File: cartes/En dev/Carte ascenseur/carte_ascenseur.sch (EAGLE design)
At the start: 22 parts, among them U1 MCP2551, U2 ADUM1250ARZ, U3 ADUM1400ARWZ

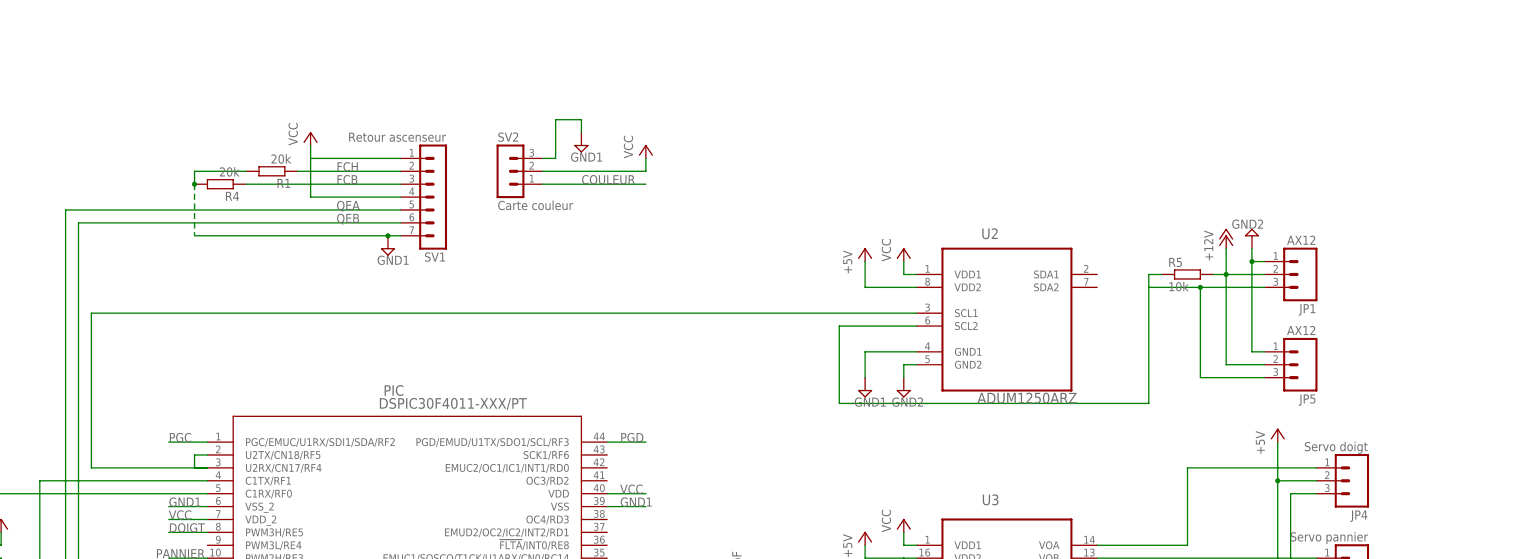
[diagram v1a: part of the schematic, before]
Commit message: Correction
Ajout de la connexion à l'alim 'dirty' et d'un LM7805 pour faire du 5V
dirty au cas où.
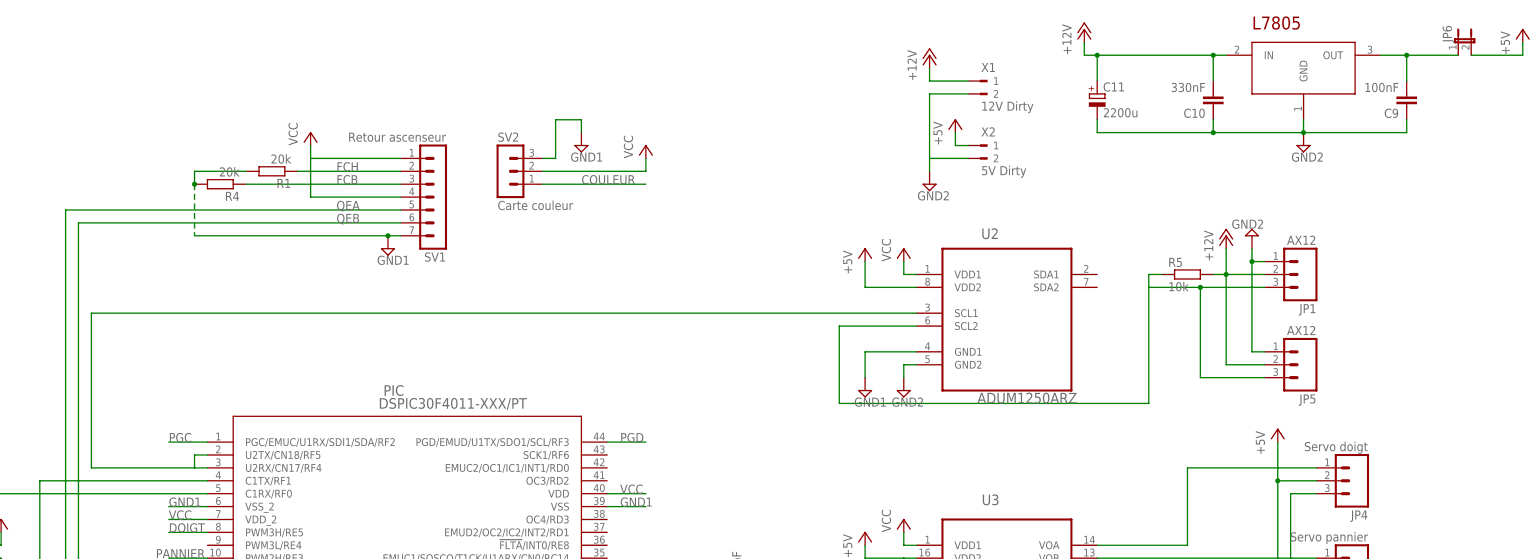
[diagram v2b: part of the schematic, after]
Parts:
- added C10: 330nF, rcl:C-EUC0805
- added C11: 2200u, rcl:CPOL-EUTT5D11
- added C9: 100nF, rcl:C-EUC0805
- added JP6: (no value), jumper:JP1E
- added U$5: L7805TO263, st-microelectronics:L7805TO263
- added X1: 12V Dirty, con-weidmueller-sl35:90-2
- added X2: 5V Dirty, con-weidmueller-sl35:90-2
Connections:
- new net N$6: C9.2, JP6.1, U$5.OUT
- net +12V: now also C10.2, C11.+, U$5.IN, X1.1
- net +5V: now also JP6.2, X2.1
- net GND2: now also C10.1, C11.-, C9.1, U$5.GND, X1.2, X2.2
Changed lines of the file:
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@@
 <part name="JP5" library="SparkFun-Connectors" deviceset="M03" device="POLAR" value="AX12"/>
 <part name="P+3" library="supply1" deviceset="VCC" device=""/>
+<part name="U$5" library="st-microelectronics" deviceset="L7805" device="TO263"/>
+<part name="C9" library="rcl" deviceset="C-EU" device="C0805" value="100nF"/>
+<part name="C10" library="rcl" deviceset="C-EU" device="C0805" value="330nF"/>
+<part name="C11" library="rcl" deviceset="CPOL-EU" device="TT5D11" value="2200u"/>
+<part name="SUPPLY9" library="supply2" deviceset="GND2" device=""/>
+<part name="P+14" library="supply1" deviceset="+12V" device=""/>
+<part name="P+15" library="supply1" deviceset="+5V" device=""/>
+<part name="X1" library="con-weidmueller-sl35" deviceset="90-2" device="" value="12V Dirty"/>
+<part name="X2" library="con-weidmueller-sl35" deviceset="90-2" device="" value="5V Dirty">
+<attribute name="MF" value=""/>
+<attribute name="MPN" value=""/>
+<attribute name="OC_FARNELL" value="unknown"/>
+<attribute name="OC_NEWARK" value="unknown"/>
+</part>
+<part name="P+16" library="supply1" deviceset="+12V" device=""/>
+<part name="SUPPLY12" library="supply2" deviceset="GND2" device=""/>
+<part name="P+17" library="supply1" deviceset="+5V" device=""/>
+<part name="JP6" library="jumper" deviceset="JP1E" device=""/>
 </parts>
 <sheets>
@@
 <instance part="JP5" gate="G$1" x="256.54" y="91.44" rot="R180"/>
 <instance part="P+3" gate="VCC" x="0" y="60.96"/>
+<instance part="U$5" gate="G$1" x="256.54" y="149.86"/>
+<instance part="C9" gate="G$1" x="276.86" y="142.24" rot="R180"/>
+<instance part="C10" gate="G$1" x="238.76" y="142.24" rot="R180"/>
+<instance part="C11" gate="G$1" x="215.9" y="144.78"/>
+<instance part="SUPPLY9" gate="G$1" x="256.54" y="134.62"/>
+<instance part="P+14" gate="1" x="213.36" y="157.48"/>
+<instance part="P+15" gate="1" x="299.72" y="157.48"/>
+<instance part="X1" gate="G$1" x="193.04" y="147.32"/>
+<instance part="X2" gate="G$1" x="193.04" y="134.62"/>
+<instance part="P+16" gate="1" x="182.88" y="152.4"/>
+<instance part="SUPPLY12" gate="G$1" x="182.88" y="127"/>
+<instance part="P+17" gate="1" x="187.96" y="139.7"/>
+<instance part="JP6" gate="A" x="287.02" y="154.94"/>
 </instances>
 <busses>
@@
 <junction x="251.46" y="50.8"/>
 </segment>
+<segment>
+<pinref part="X2" gate="G$1" pin="1"/>
+<wire x1="190.5" y1="134.62" x2="187.96" y2="134.62" width="0.1524" layer="91"/>
+<wire x1="187.96" y1="134.62" x2="187.96" y2="137.16" width="0.1524" layer="91"/>
+<pinref part="P+17" gate="1" pin="+5V"/>
+</segment>
+<segment>
+<pinref part="JP6" gate="A" pin="2"/>
+<pinref part="P+15" gate="1" pin="+5V"/>
+<wire x1="289.56" y1="152.4" x2="299.72" y2="152.4" width="0.1524" layer="91"/>
+<wire x1="299.72" y1="152.4" x2="299.72" y2="154.94" width="0.1524" layer="91"/>
+</segment>
 </net>
 <net name="GND1" class="0">
@@
 <junction x="254" y="30.48"/>
 </segment>
+<segment>
+<pinref part="C9" gate="G$1" pin="1"/>
+<wire x1="276.86" y1="139.7" x2="276.86" y2="137.16" width="0.1524" layer="91"/>
+<wire x1="276.86" y1="137.16" x2="256.54" y2="137.16" width="0.1524" layer="91"/>
+<pinref part="U$5" gate="G$1" pin="GND"/>
+<wire x1="256.54" y1="139.7" x2="256.54" y2="137.16" width="0.1524" layer="91"/>
+<pinref part="C10" gate="G$1" pin="1"/>
+<wire x1="256.54" y1="137.16" x2="238.76" y2="137.16" width="0.1524" layer="91"/>
+<wire x1="238.76" y1="137.16" x2="238.76" y2="139.7" width="0.1524" layer="91"/>
+<junction x="256.54" y="137.16"/>
+<pinref part="C11" gate="G$1" pin="-"/>
+<wire x1="215.9" y1="139.7" x2="215.9" y2="137.16" width="0.1524" layer="91"/>
+<wire x1="215.9" y1="137.16" x2="238.76" y2="137.16" width="0.1524" layer="91"/>
+<junction x="238.76" y="137.16"/>
+<pinref part="SUPPLY9" gate="G$1" pin="GND2"/>
+</segment>
+<segment>
+<pinref part="X1" gate="G$1" pin="2"/>
+<wire x1="190.5" y1="144.78" x2="182.88" y2="144.78" width="0.1524" layer="91"/>
+<wire x1="182.88" y1="144.78" x2="182.88" y2="132.08" width="0.1524" layer="91"/>
+<pinref part="X2" gate="G$1" pin="2"/>
+<wire x1="190.5" y1="132.08" x2="182.88" y2="132.08" width="0.1524" layer="91"/>
+<wire x1="182.88" y1="132.08" x2="182.88" y2="129.54" width="0.1524" layer="91"/>
+<pinref part="SUPPLY12" gate="G$1" pin="GND2"/>
+</segment>
 </net>
 <net name="N$1" class="0">
@@
 <wire x1="38.1" y1="73.66" x2="38.1" y2="71.12" width="0.1524" layer="91"/>
 <pinref part="PIC" gate="A" pin="U2RX/CN17/RF4"/>
-<wire x1="38.1" y1="71.12" x2="40.64" y2="71.12" width="0.1524" layer="91"/>
-<wire x1="40.64" y1="71.12" x2="17.78" y2="71.12" width="0.1524" layer="91"/>
+<wire x1="40.64" y1="71.12" x2="38.1" y2="71.12" width="0.1524" layer="91"/>
+<wire x1="38.1" y1="71.12" x2="17.78" y2="71.12" width="0.1524" layer="91"/>
 <wire x1="17.78" y1="71.12" x2="17.78" y2="101.6" width="0.1524" layer="91"/>
 <pinref part="U2" gate="A" pin="SCL1"/>
@@
 <wire x1="241.3" y1="109.22" x2="238.76" y2="109.22" width="0.1524" layer="91"/>
 </segment>
-</net>
+<segment>
+<pinref part="U$5" gate="G$1" pin="IN"/>
+<wire x1="241.3" y1="152.4" x2="238.76" y2="152.4" width="0.1524" layer="91"/>
+<pinref part="C10" gate="G$1" pin="2"/>
+<wire x1="238.76" y1="152.4" x2="215.9" y2="152.4" width="0.1524" layer="91"/>
+<wire x1="215.9" y1="152.4" x2="213.36" y2="152.4" width="0.1524" layer="91"/>
+<wire x1="238.76" y1="147.32" x2="238.76" y2="152.4" width="0.1524" layer="91"/>
+<junction x="238.76" y="152.4"/>
+<pinref part="C11" gate="G$1" pin="+"/>
+<wire x1="215.9" y1="147.32" x2="215.9" y2="152.4" width="0.1524" layer="91"/>
+<junction x="215.9" y="152.4"/>
+<pinref part="P+14" gate="1" pin="+12V"/>
+<wire x1="213.36" y1="154.94" x2="213.36" y2="152.4" width="0.1524" layer="91"/>
+</segment>
+<segment>
+<pinref part="X1" gate="G$1" pin="1"/>
+<wire x1="190.5" y1="147.32" x2="182.88" y2="147.32" width="0.1524" layer="91"/>
+<wire x1="182.88" y1="147.32" x2="182.88" y2="149.86" width="0.1524" layer="91"/>
+<pinref part="P+16" gate="1" pin="+12V"/>
+</segment>
+</net>
+<net name="N$6" class="0">
+<segment>
+<pinref part="U$5" gate="G$1" pin="OUT"/>
+<wire x1="271.78" y1="152.4" x2="276.86" y2="152.4" width="0.1524" layer="91"/>
+<pinref part="C9" gate="G$1" pin="2"/>
+<wire x1="276.86" y1="152.4" x2="287.02" y2="152.4" width="0.1524" layer="91"/>
+<wire x1="276.86" y1="147.32" x2="276.86" y2="152.4" width="0.1524" layer="91"/>
+<junction x="276.86" y="152.4"/>
+<pinref part="JP6" gate="A" pin="1"/>
+</segment>
+</net>

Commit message: Correction carte ascenseur
Ajout des leds d'indication de présence de tension, 5V, 5V dirty, 12V
dirty
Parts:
- added LED_12V, LED_5V, LED_5V1: (no value), adafruit:LEDCHIPLED_0805
- added R6, R7, R8: 1k, SparkFun-Passives:RESISTOR0805-RES
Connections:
- new net N$11: LED_12V.A, R7.2
- new net N$12: LED_5V1.A, R8.2
- new net N$2: LED_5V.A, R6.2
- new net N$5: LED_12V.C, LED_5V.C
- net +12V: now also R7.1
- net +5V: now also R6.1
- net DOIGT: now also U3.VIB; no longer U3.VIA
- net GND1: now also LED_5V1.C
- net LANCEUR: now also U3.VIA; no longer U3.VIC
- net PANNIER: now also U3.VIC; no longer U3.VIB
- net VCC: now also R8.1
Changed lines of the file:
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@@
 <layer number="54" name="bGND_GNDA" color="1" fill="9" visible="no" active="no"/>
 <layer number="56" name="wert" color="7" fill="1" visible="no" active="no"/>
+<layer number="57" name="tCAD" color="7" fill="1" visible="no" active="no"/>
 <layer number="91" name="Nets" color="2" fill="1" visible="yes" active="yes"/>
 <layer number="92" name="Busses" color="1" fill="1" visible="yes" active="yes"/>
@@
 <layer number="108" name="tplace-old" color="10" fill="1" visible="yes" active="yes"/>
 <layer number="109" name="ref-old" color="11" fill="1" visible="yes" active="yes"/>
+<layer number="110" name="fp0" color="7" fill="1" visible="no" active="yes"/>
+<layer number="111" name="LPC17xx" color="7" fill="1" visible="yes" active="yes"/>
+<layer number="112" name="tSilk" color="7" fill="1" visible="yes" active="yes"/>
 <layer number="116" name="Patch_BOT" color="9" fill="4" visible="yes" active="yes"/>
 <layer number="121" name="_tsilk" color="7" fill="1" visible="yes" active="yes"/>
 <layer number="122" name="_bsilk" color="7" fill="1" visible="yes" active="yes"/>
+<layer number="123" name="tTestmark" color="7" fill="1" visible="no" active="yes"/>
+<layer number="124" name="bTestmark" color="7" fill="1" visible="no" active="yes"/>
 <layer number="125" name="_tNames" color="7" fill="1" visible="yes" active="yes"/>
+<layer number="126" name="_bNames" color="7" fill="1" visible="yes" active="yes"/>
+<layer number="127" name="_tValues" color="7" fill="1" visible="yes" active="yes"/>
+<layer number="128" name="_bValues" color="7" fill="1" visible="yes" active="yes"/>
+<layer number="131" name="tAdjust" color="7" fill="1" visible="no" active="yes"/>
+<layer number="132" name="bAdjust" color="7" fill="1" visible="no" active="yes"/>
 <layer number="144" name="Drill_legend" color="7" fill="1" visible="yes" active="yes"/>
+<layer number="150" name="Notes" color="7" fill="1" visible="no" active="yes"/>
 <layer number="151" name="HeatSink" color="7" fill="1" visible="yes" active="yes"/>
+<layer number="152" name="_bDocu" color="7" fill="1" visible="yes" active="yes"/>
+<layer number="153" name="FabDoc1" color="6" fill="1" visible="no" active="no"/>
+<layer number="154" name="FabDoc2" color="2" fill="1" visible="no" active="no"/>
+<layer number="155" name="FabDoc3" color="7" fill="15" visible="no" active="no"/>
 <layer number="199" name="Contour" color="7" fill="1" visible="yes" active="yes"/>
 <layer number="200" name="200bmp" color="1" fill="10" visible="no" active="no"/>
@@
 <layer number="223" name="223bmp" color="24" fill="1" visible="no" active="no"/>
 <layer number="224" name="224bmp" color="25" fill="1" visible="no" active="no"/>
+<layer number="248" name="Housing" color="7" fill="1" visible="yes" active="yes"/>
+<layer number="249" name="Edge" color="7" fill="1" visible="yes" active="yes"/>
 <layer number="250" name="Descript" color="3" fill="1" visible="no" active="no"/>
 <layer number="251" name="SMDround" color="12" fill="11" visible="no" active="no"/>
@@
 <part name="P+17" library="supply1" deviceset="+5V" device=""/>
 <part name="JP6" library="jumper" deviceset="JP1E" device=""/>
+<part name="LED_5V" library="adafruit" deviceset="LED" device="CHIPLED_0805"/>
+<part name="R6" library="SparkFun-Passives" deviceset="RESISTOR" device="0805-RES" value="1k">
+<attribute name="MF" value=""/>
+<attribute name="MPN" value=""/>
+<attribute name="OC_FARNELL" value="unknown"/>
+</part>
+<part name="P+18" library="supply1" deviceset="+5V" device=""/>
+<part name="SUPPLY16" library="supply2" deviceset="GND2" device=""/>
+<part name="LED_12V" library="adafruit" deviceset="LED" device="CHIPLED_0805"/>
+<part name="R7" library="SparkFun-Passives" deviceset="RESISTOR" device="0805-RES" value="1k">
+<attribute name="MF" value=""/>
+<attribute name="MPN" value=""/>
+<attribute name="OC_FARNELL" value="unknown"/>
+</part>
+<part name="P+19" library="supply1" deviceset="+12V" device=""/>
+<part name="LED_5V1" library="adafruit" deviceset="LED" device="CHIPLED_0805"/>
+<part name="R8" library="SparkFun-Passives" deviceset="RESISTOR" device="0805-RES" value="1k">
+<attribute name="MF" value=""/>
+<attribute name="MPN" value=""/>
+<attribute name="OC_FARNELL" value="unknown"/>
+</part>
+<part name="P+20" library="supply1" deviceset="VCC" device=""/>
+<part name="SUPPLY18" library="supply2" deviceset="GND1" device=""/>
 </parts>
 <sheets>
@@
 <instance part="P+17" gate="1" x="187.96" y="139.7"/>
 <instance part="JP6" gate="A" x="287.02" y="154.94"/>
+<instance part="LED_5V" gate="G$1" x="317.5" y="111.76"/>
+<instance part="R6" gate="G$1" x="317.5" y="121.92" rot="R270">
+<attribute name="OC_FARNELL" x="317.5" y="121.92" size="1.778" layer="96" rot="R180" display="off"/>
+<attribute name="MF" x="317.5" y="121.92" size="1.778" layer="96" rot="R180" display="off"/>
+<attribute name="MPN" x="317.5" y="121.92" size="1.778" layer="96" rot="R180" display="off"/>
+</instance>
+<instance part="P+18" gate="1" x="317.5" y="134.62"/>
+<instance part="SUPPLY16" gate="G$1" x="317.5" y="99.06"/>
+<instance part="LED_12V" gate="G$1" x="330.2" y="111.76"/>
+<instance part="R7" gate="G$1" x="330.2" y="121.92" rot="R270">
+<attribute name="OC_FARNELL" x="330.2" y="121.92" size="1.778" layer="96" rot="R180" display="off"/>
+<attribute name="MF" x="330.2" y="121.92" size="1.778" layer="96" rot="R180" display="off"/>
+<attribute name="MPN" x="330.2" y="121.92" size="1.778" layer="96" rot="R180" display="off"/>
+</instance>
+<instance part="P+19" gate="1" x="330.2" y="134.62"/>
+<instance part="LED_5V1" gate="G$1" x="-104.14" y="48.26"/>
+<instance part="R8" gate="G$1" x="-104.14" y="58.42" rot="R270">
+<attribute name="OC_FARNELL" x="-104.14" y="58.42" size="1.778" layer="96" rot="R180" display="off"/>
+<attribute name="MF" x="-104.14" y="58.42" size="1.778" layer="96" rot="R180" display="off"/>
+<attribute name="MPN" x="-104.14" y="58.42" size="1.778" layer="96" rot="R180" display="off"/>
+</instance>
+<instance part="P+20" gate="VCC" x="-104.14" y="68.58"/>
+<instance part="SUPPLY18" gate="G$1" x="-104.14" y="38.1"/>
 </instances>
 <busses>
@@
 <wire x1="299.72" y1="152.4" x2="299.72" y2="154.94" width="0.1524" layer="91"/>
 </segment>
+<segment>
+<pinref part="R6" gate="G$1" pin="1"/>
+<wire x1="317.5" y1="127" x2="317.5" y2="132.08" width="0.1524" layer="91"/>
+<pinref part="P+18" gate="1" pin="+5V"/>
+</segment>
 </net>
 <net name="GND1" class="0">
@@
 <wire x1="-7.62" y1="53.34" x2="0" y2="53.34" width="0.1524" layer="91"/>
 <wire x1="0" y1="53.34" x2="0" y2="50.8" width="0.1524" layer="91"/>
+</segment>
+<segment>
+<pinref part="LED_5V1" gate="G$1" pin="C"/>
+<wire x1="-104.14" y1="43.18" x2="-104.14" y2="40.64" width="0.1524" layer="91"/>
+<pinref part="SUPPLY18" gate="G$1" pin="GND1"/>
 </segment>
 </net>
@@
 <pinref part="U1" gate="G$1" pin="VDD"/>
 <wire x1="-5.08" y1="55.88" x2="-7.62" y2="55.88" width="0.1524" layer="91"/>
+</segment>
+<segment>
+<pinref part="P+20" gate="VCC" pin="VCC"/>
+<pinref part="R8" gate="G$1" pin="1"/>
+<wire x1="-104.14" y1="66.04" x2="-104.14" y2="63.5" width="0.1524" layer="91"/>
 </segment>
 </net>
@@
 </segment>
 <segment>
-<pinref part="U3" gate="A" pin="VIA"/>
-<wire x1="180.34" y1="43.18" x2="172.72" y2="43.18" width="0.1524" layer="91"/>
-<label x="172.72" y="43.18" size="1.778" layer="96"/>
+<label x="167.64" y="40.64" size="1.778" layer="96"/>
+<pinref part="U3" gate="A" pin="VIB"/>
+<wire x1="167.64" y1="40.64" x2="180.34" y2="40.64" width="0.1524" layer="91"/>
 </segment>
 </net>
@@
 </segment>
 <segment>
-<pinref part="U3" gate="A" pin="VIB"/>
-<wire x1="180.34" y1="40.64" x2="172.72" y2="40.64" width="0.1524" layer="91"/>
-<label x="170.18" y="40.64" size="1.778" layer="96"/>
+<pinref part="U3" gate="A" pin="VIC"/>
+<wire x1="167.64" y1="38.1" x2="180.34" y2="38.1" width="0.1524" layer="91"/>
+<label x="167.64" y="38.1" size="1.778" layer="95"/>
 </segment>
 </net>
 <net name="LANCEUR" class="0">
 <segment>
-<pinref part="U3" gate="A" pin="VIC"/>
-<wire x1="180.34" y1="38.1" x2="172.72" y2="38.1" width="0.1524" layer="91"/>
-<label x="170.18" y="38.1" size="1.778" layer="96"/>
+<label x="167.64" y="43.18" size="1.778" layer="96"/>
+<pinref part="U3" gate="A" pin="VIA"/>
+<wire x1="167.64" y1="43.18" x2="180.34" y2="43.18" width="0.1524" layer="91"/>
 </segment>
 <segment>
@@
 <pinref part="P+16" gate="1" pin="+12V"/>
 </segment>
+<segment>
+<pinref part="P+19" gate="1" pin="+12V"/>
+<pinref part="R7" gate="G$1" pin="1"/>
+<wire x1="330.2" y1="132.08" x2="330.2" y2="127" width="0.1524" layer="91"/>
+</segment>
 </net>
 <net name="N$6" class="0">
@@
 </segment>
 </net>
+<net name="N$2" class="0">
+<segment>
+<pinref part="LED_5V" gate="G$1" pin="A"/>
+<pinref part="R6" gate="G$1" pin="2"/>
+<wire x1="317.5" y1="114.3" x2="317.5" y2="116.84" width="0.1524" layer="91"/>
+</segment>
+</net>
+<net name="N$5" class="0">
+<segment>
+<pinref part="LED_5V" gate="G$1" pin="C"/>
+<wire x1="317.5" y1="106.68" x2="317.5" y2="104.14" width="0.1524" layer="91"/>
+<pinref part="SUPPLY16" gate="G$1" pin="GND2"/>
+<pinref part="LED_12V" gate="G$1" pin="C"/>
+<wire x1="317.5" y1="104.14" x2="317.5" y2="101.6" width="0.1524" layer="91"/>
+<wire x1="317.5" y1="104.14" x2="330.2" y2="104.14" width="0.1524" layer="91"/>
+<wire x1="330.2" y1="104.14" x2="330.2" y2="106.68" width="0.1524" layer="91"/>
+</segment>
+</net>
+<net name="N$11" class="0">
+<segment>
+<pinref part="LED_12V" gate="G$1" pin="A"/>
+<pinref part="R7" gate="G$1" pin="2"/>
+<wire x1="330.2" y1="114.3" x2="330.2" y2="116.84" width="0.1524" layer="91"/>
+</segment>
+</net>
+<net name="N$12" class="0">
+<segment>
+<pinref part="R8" gate="G$1" pin="2"/>
+<pinref part="LED_5V1" gate="G$1" pin="A"/>
+<wire x1="-104.14" y1="53.34" x2="-104.14" y2="50.8" width="0.1524" layer="91"/>
+</segment>
+</net>
